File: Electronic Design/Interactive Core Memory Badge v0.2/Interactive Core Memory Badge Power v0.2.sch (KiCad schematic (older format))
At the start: 15 parts, among them Q21 MMBT4401LT1G, SW3 SW_DPDT_x2, U1 Micro_LiPo_Charger

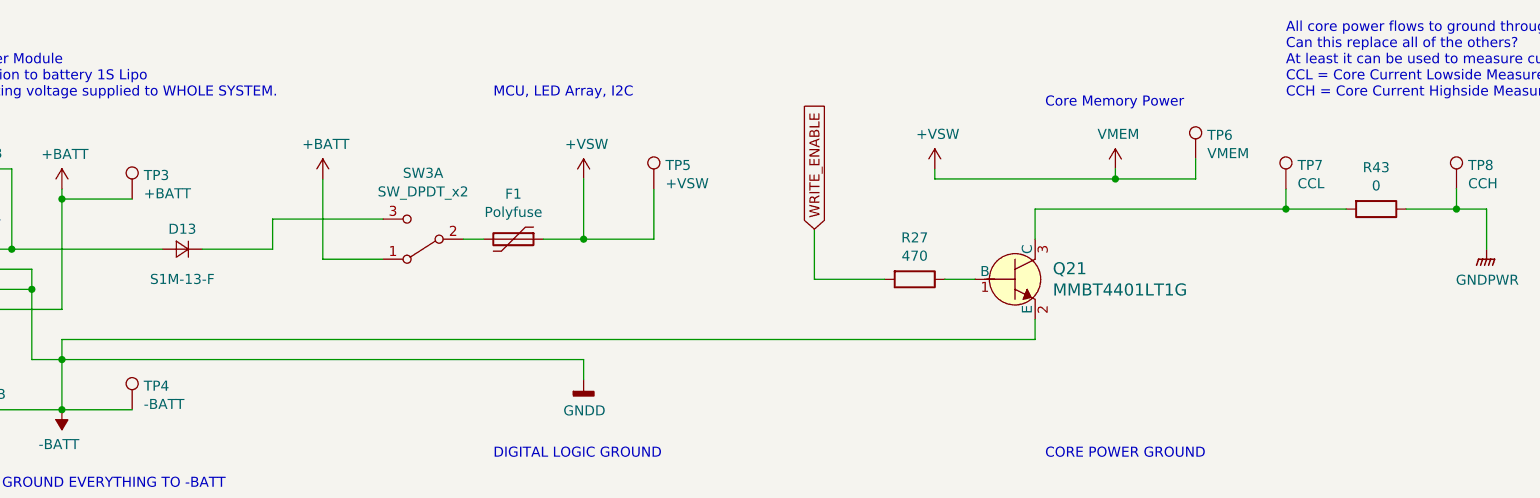
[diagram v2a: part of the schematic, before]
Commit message: Tweaks to V0.2 schematic and layout from notes.
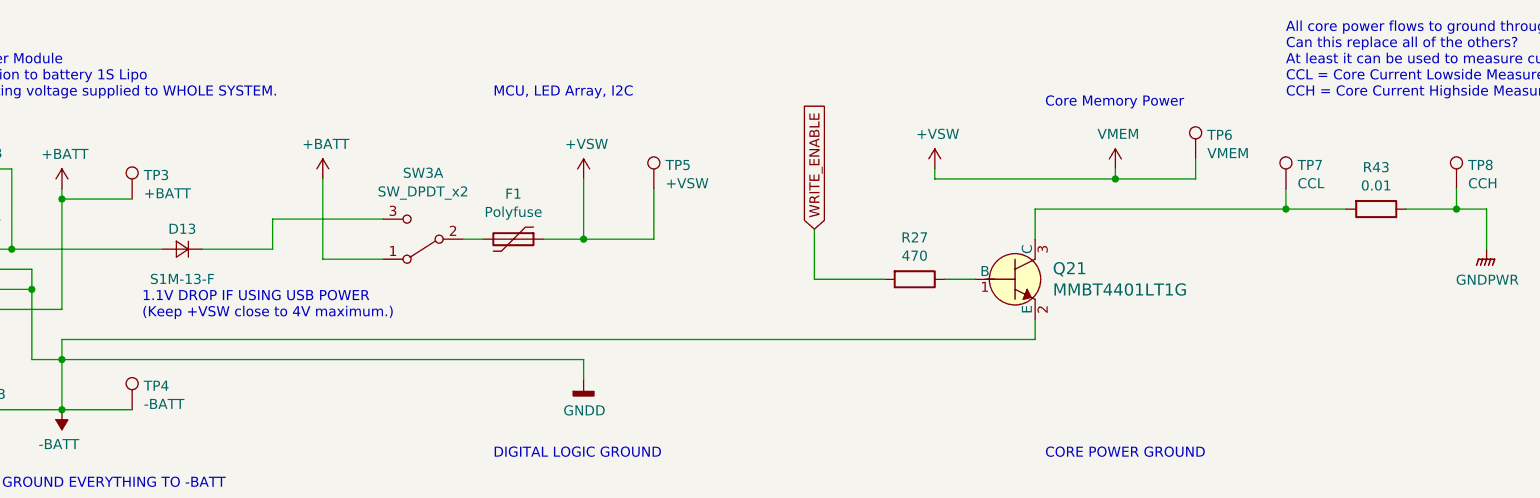
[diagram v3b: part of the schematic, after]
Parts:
- R43: value 0 -> 0.01
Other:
- note added: "1.1V DROP IF USING USB POWER\n(Keep +VSW close to 4V maximum.)"
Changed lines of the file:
@@
 AR Path="/5D254AE8/5D4B5807" Ref="R43"  Part="1"
 F 0 "R43" V 8743 1800 50  0000 C CNN
-F 1 "0" V 8834 1800 50  0000 C CNN
+F 1 "0.01" V 8834 1800 50  0000 C CNN
 F 2 "Resistor_SMD:R_0805_2012Metric" V 8880 1800 50  0001 C CNN
 F 3 "~" H 8950 1800 50  0001 C CNN
@@
 	2900 2000 2150 2000
 Connection ~ 2150 2000
+Text Notes 2800 2350 0    50   ~ 0
+1.1V DROP IF USING USB POWER\n(Keep +VSW close to 4V maximum.)
 $EndSCHEMATC
